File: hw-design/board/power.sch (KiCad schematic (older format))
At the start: 14 parts, among them CN1 CONN_02X02, CN2 CONN_02X02, U1 AP1117E50, U2 AP1117E33

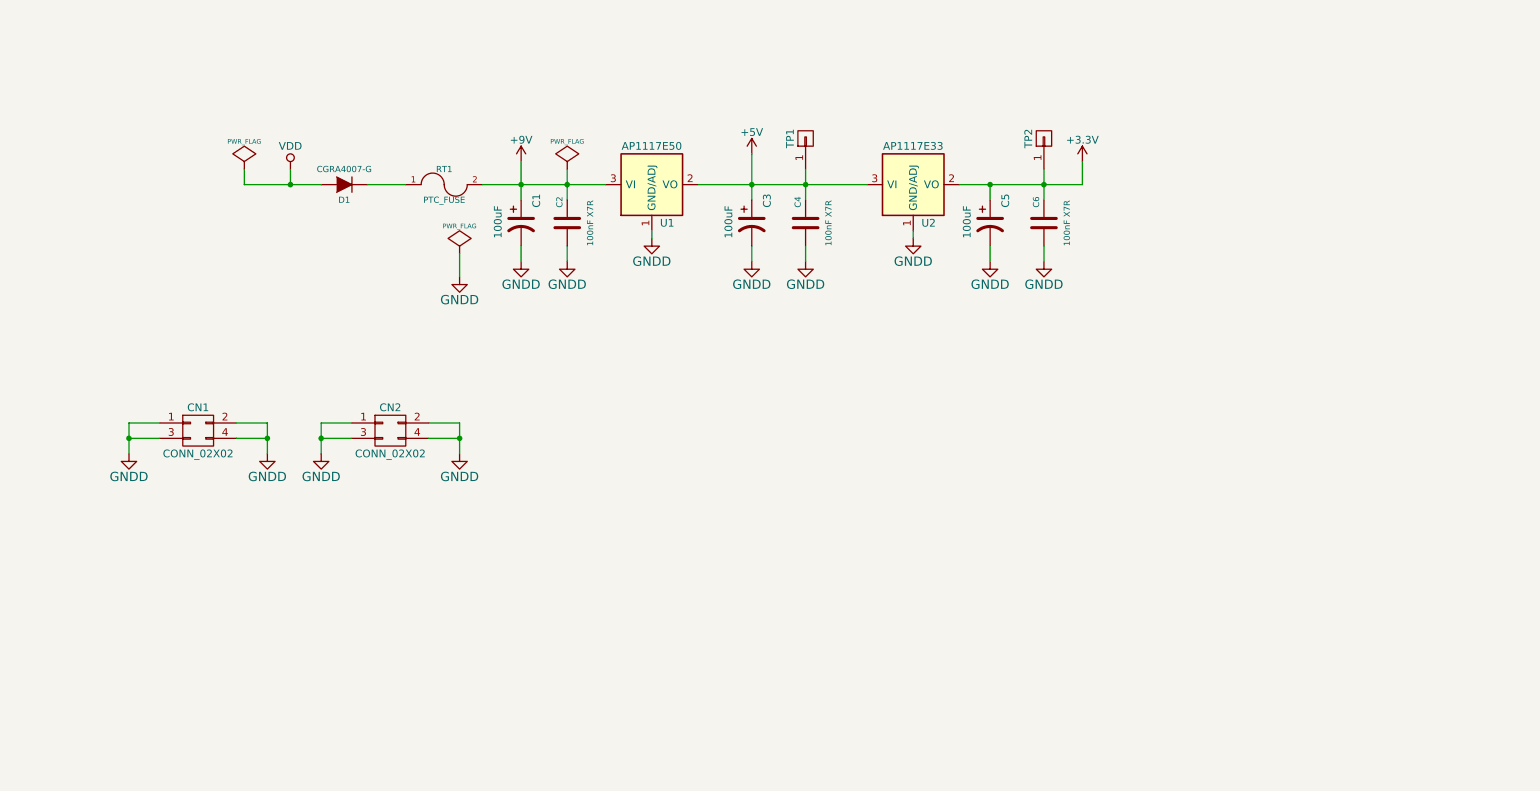
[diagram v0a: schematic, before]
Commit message: sch: load switch circuit sketch
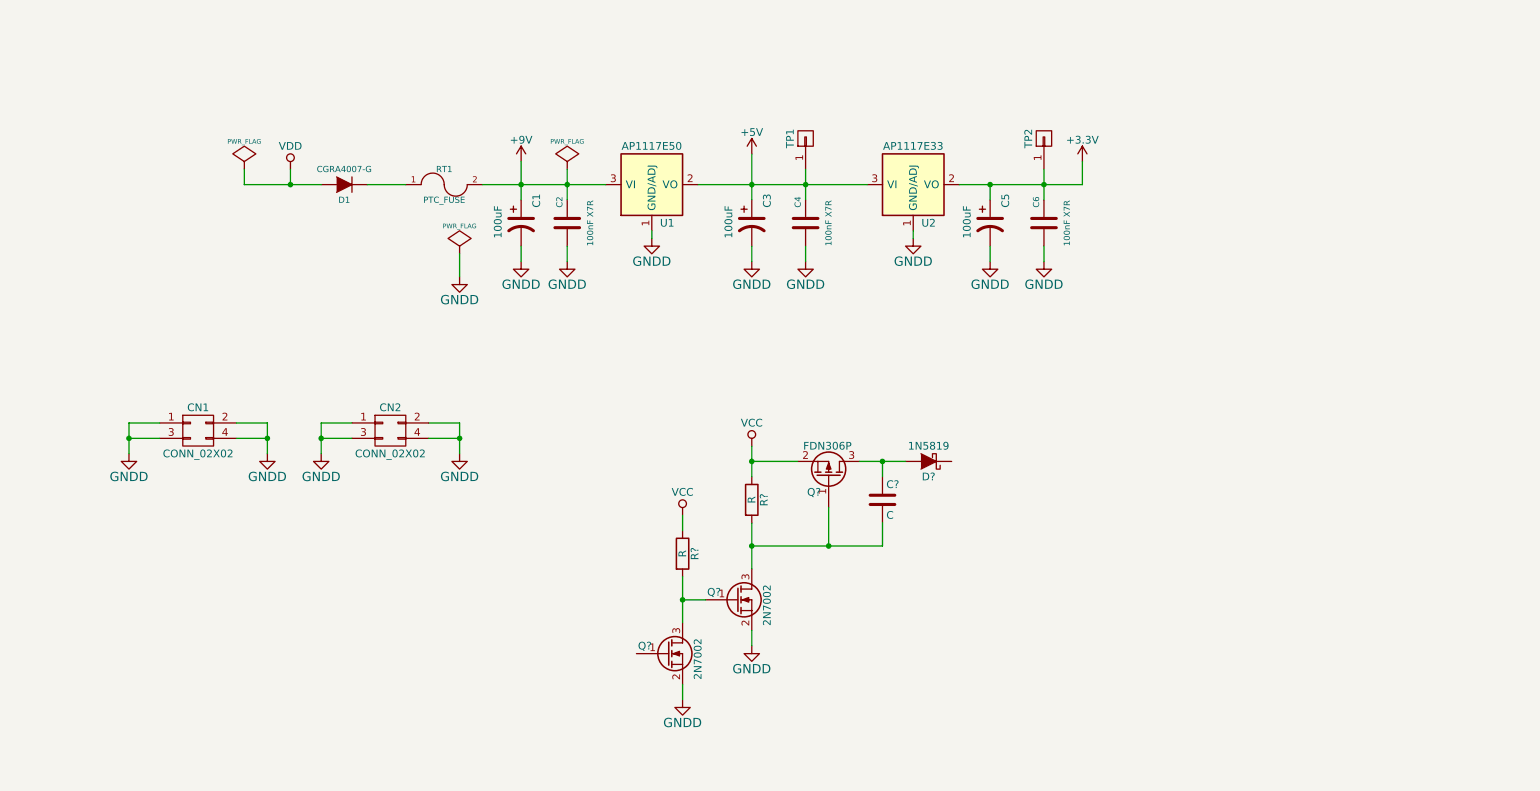
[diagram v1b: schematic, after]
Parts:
- added C?: C, symbol C
- added D?: 1N5819, symbol D_Schottky
- added Q?: FDN306P, symbol Q_PMOS_GSD
- added Q? (x2): 2N7002, symbol Q_NMOS_GSD
- added R? (x2): R, symbol R
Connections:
- net GNDD: now also Q?.2 (S), Q?.2 (S)
- new net: C?.2, Q?.1 (G), Q?.3 (D), R?.2
- new net: C?.1, D?.2 (A), Q?.3 (D)
- new net: Q?.1 (G), Q?.3 (D), R?.2
- new net VCC: Q?.2 (S), R?.1, R?.1
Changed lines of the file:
@@
 EESchema Schematic File Version 2
+LIBS:conn
+LIBS:device
+LIBS:interface
+LIBS:power
 LIBS:regul
-LIBS:power
-LIBS:device
 LIBS:transistors
 LIBS:nxp_armmcu
-LIBS:conn
-LIBS:interface
 LIBS:expression-pedal-cache
 EELAYER 25 0
@@
 	7100 2000 7100 2100
 Wire Wire Line
-	7450 1900 7450 2100
+	7450 1900 7450 2000
+Wire Wire Line
+	7450 2000 7450 2100
 Connection ~ 7100 2000
 Connection ~ 5550 2000
@@
 	4050 2400 4050 2500
 Wire Wire Line
-	4050 1850 4050 2100
+	4050 1850 4050 2000
+Wire Wire Line
+	4050 2000 4050 2100
 Connection ~ 4050 2000
 Wire Wire Line
 	4350 2400 4350 2500
 Wire Wire Line
-	4350 1900 4350 2100
+	4350 1900 4350 2000
+Wire Wire Line
+	4350 2000 4350 2100
 Connection ~ 4350 2000
 Wire Wire Line
 	3050 2000 3300 2000
 Wire Wire Line
-	5900 1900 5900 2100
+	5900 1900 5900 2000
+Wire Wire Line
+	5900 2000 5900 2100
 Connection ~ 5900 2000
 Wire Wire Line
-	5550 1800 5550 2100
-Wire Wire Line
-	2250 2000 2750 2000
+	5550 1800 5550 2000
+Wire Wire Line
+	5550 2000 5550 2100
+Wire Wire Line
+	2250 2000 2550 2000
+Wire Wire Line
+	2550 2000 2750 2000
 Wire Wire Line
 	3650 2450 3650 2600
@@
 	1500 3650 1700 3650
 Wire Wire Line
-	1500 3550 1500 3750
+	1500 3550 1500 3650
+Wire Wire Line
+	1500 3650 1500 3750
 Wire Wire Line
 	1500 3550 1700 3550
@@
 	2200 3650 2400 3650
 Wire Wire Line
-	2400 3550 2400 3750
+	2400 3550 2400 3650
+Wire Wire Line
+	2400 3650 2400 3750
 Wire Wire Line
 	2200 3550 2400 3550
 Connection ~ 2400 3650
 Wire Wire Line
-	3650 3550 3650 3750
+	3650 3550 3650 3650
+Wire Wire Line
+	3650 3650 3650 3750
 Wire Wire Line
 	3450 3650 3650 3650
@@
 	2750 3650 2950 3650
 Wire Wire Line
-	2750 3550 2750 3750
+	2750 3550 2750 3650
+Wire Wire Line
+	2750 3650 2750 3750
 Wire Wire Line
 	2750 3550 2950 3550
@@
 $EndComp
 Wire Wire Line
-	5200 2000 6300 2000
+	5200 2000 5550 2000
+Wire Wire Line
+	5550 2000 5900 2000
+Wire Wire Line
+	5900 2000 6300 2000
 $Comp
 L GNDD #PWR019
@@
 $EndComp
 Wire Wire Line
-	3800 2000 4600 2000
-Wire Wire Line
-	6900 2000 7700 2000
+	3800 2000 4050 2000
+Wire Wire Line
+	4050 2000 4350 2000
+Wire Wire Line
+	4350 2000 4600 2000
+Wire Wire Line
+	6900 2000 7100 2000
+Wire Wire Line
+	7100 2000 7450 2000
+Wire Wire Line
+	7450 2000 7700 2000
 $Comp
 L +3.3V #PWR?
@@
 	1    0    0    -1
 $EndComp
+$Comp
+L Q_PMOS_GSD Q?
+U 1 1 5576EC7B
+P 6050 3900
+F 0 "Q?" V 5950 3850 50  0000 R CNN
+F 1 "FDN306P" V 6250 4050 50  0000 R CNN
+F 2 "" H 6250 4000 29  0000 C CNN
+F 3 "" H 6050 3900 60  0000 C CNN
+	1    6050 3900
+	0    1    -1   0
+$EndComp
+$Comp
+L D_Schottky D?
+U 1 1 5576EF8F
+P 6700 3800
+F 0 "D?" H 6700 3900 50  0000 C CNN
+F 1 "1N5819" H 6700 3700 50  0000 C CNN
+F 2 "" H 6700 3800 60  0000 C CNN
+F 3 "" H 6700 3800 60  0000 C CNN
+	1    6700 3800
+	-1   0    0    1
+$EndComp
+$Comp
+L R R?
+U 1 1 5576FA4A
+P 5550 4050
+F 0 "R?" V 5630 4050 50  0000 C CNN
+F 1 "R" V 5550 4050 50  0000 C CNN
+F 2 "" V 5480 4050 30  0000 C CNN
+F 3 "" H 5550 4050 30  0000 C CNN
+	1    5550 4050
+	1    0    0    -1
+$EndComp
+$Comp
+L VCC #PWR?
+U 1 1 55770535
+P 5550 3700
+F 0 "#PWR?" H 5550 3550 50  0001 C CNN
+F 1 "VCC" H 5550 3850 50  0000 C CNN
+F 2 "" H 5550 3700 60  0000 C CNN
+F 3 "" H 5550 3700 60  0000 C CNN
+	1    5550 3700
+	1    0    0    -1
+$EndComp
+Wire Wire Line
+	5550 3700 5550 3800
+Wire Wire Line
+	5550 3800 5550 3900
+Wire Wire Line
+	5850 3800 5550 3800
+Connection ~ 5550 3800
+Wire Wire Line
+	6250 3800 6400 3800
+Wire Wire Line
+	6400 3800 6550 3800
+$Comp
+L Q_NMOS_GSD Q?
+U 1 1 55771A8F
+P 5450 4700
+F 0 "Q?" H 5350 4750 50  0000 R CNN
+F 1 "2N7002" V 5650 4800 50  0000 R CNN
+F 2 "" H 5650 4800 29  0000 C CNN
+F 3 "" H 5450 4700 60  0000 C CNN
+	1    5450 4700
+	1    0    0    -1
+$EndComp
+$Comp
+L Q_NMOS_GSD Q?
+U 1 1 55771C8E
+P 5000 5050
+F 0 "Q?" H 4900 5100 50  0000 R CNN
+F 1 "2N7002" V 5200 5150 50  0000 R CNN
+F 2 "" H 5200 5150 29  0000 C CNN
+F 3 "" H 5000 5050 60  0000 C CNN
+	1    5000 5050
+	1    0    0    -1
+$EndComp
+$Comp
+L GNDD #PWR?
+U 1 1 557724D6
+P 5100 5350
+F 0 "#PWR?" H 5100 5100 60  0001 C CNN
+F 1 "GNDD" H 5100 5200 60  0000 C CNN
+F 2 "" H 5100 5350 60  0000 C CNN
+F 3 "" H 5100 5350 60  0000 C CNN
+	1    5100 5350
+	1    0    0    -1
+$EndComp
+Wire Wire Line
+	5100 5350 5100 5250
+Wire Wire Line
+	5100 4550 5100 4700
+Wire Wire Line
+	5100 4700 5100 4850
+Wire Wire Line
+	5100 4700 5250 4700
+$Comp
+L GNDD #PWR?
+U 1 1 55772F70
+P 5550 5000
+F 0 "#PWR?" H 5550 4750 60  0001 C CNN
+F 1 "GNDD" H 5550 4850 60  0000 C CNN
+F 2 "" H 5550 5000 60  0000 C CNN
+F 3 "" H 5550 5000 60  0000 C CNN
+	1    5550 5000
+	1    0    0    -1
+$EndComp
+Wire Wire Line
+	5550 5000 5550 4900
+$Comp
+L R R?
+U 1 1 55773BAE
+P 5100 4400
+F 0 "R?" V 5180 4400 50  0000 C CNN
+F 1 "R" V 5100 4400 50  0000 C CNN
+F 2 "" V 5030 4400 30  0000 C CNN
+F 3 "" H 5100 4400 30  0000 C CNN
+	1    5100 4400
+	1    0    0    -1
+$EndComp
+Connection ~ 5100 4700
+Wire Wire Line
+	5550 4200 5550 4350
+Wire Wire Line
+	5550 4350 5550 4500
+Wire Wire Line
+	5550 4350 6050 4350
+Wire Wire Line
+	6050 4350 6400 4350
+Wire Wire Line
+	6050 4350 6050 4100
+Connection ~ 5550 4350
+$Comp
+L VCC #PWR?
+U 1 1 55774D84
+P 5100 4150
+F 0 "#PWR?" H 5100 4000 50  0001 C CNN
+F 1 "VCC" H 5100 4300 50  0000 C CNN
+F 2 "" H 5100 4150 60  0000 C CNN
+F 3 "" H 5100 4150 60  0000 C CNN
+	1    5100 4150
+	1    0    0    -1
+$EndComp
+$Comp
+L C C?
+U 1 1 55779079
+P 6400 4050
+F 0 "C?" H 6425 4150 50  0000 L CNN
+F 1 "C" H 6425 3950 50  0000 L CNN
+F 2 "" H 6438 3900 30  0000 C CNN
+F 3 "" H 6400 4050 60  0000 C CNN
+	1    6400 4050
+	1    0    0    -1
+$EndComp
+Wire Wire Line
+	6400 3900 6400 3800
+Connection ~ 6400 3800
+Wire Wire Line
+	6400 4350 6400 4200
+Connection ~ 6050 4350
+Wire Wire Line
+	5100 4250 5100 4150
 $EndSCHEMATC

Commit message: power circuit done
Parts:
- removed CN1, CN2: CONN_02X02, MOD_Footprints:CONN_PANNEL, symbol CONN_02X02
- removed TP1, TP2: ~, Pin_Headers:Pin_Header_Straight_1x01, symbol CONN_01X01
- removed U1: AP1117E50, SMD_Packages:SOT-223, symbol AP1117E50
- removed U2: AP1117E33, SMD_Packages:SOT-223, symbol AP1117E33
- added C?: 100nF X7R, Capacitors_SMD:C_0603, symbol C
- added D?: 1N5819, symbol D_Schottky
- added R? (x2): R, symbol R
- added U?: NCP1117DT50G, symbol NCP1117ST50T3G
- added U?: NCP1117DT33G, symbol NCP1117ST33T3G
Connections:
- net +3V3: now also U?.2 (VO)
- net +5V: now also D?.1 (K), C?.1, D?.1 (K), U?.3 (VI); no longer C3.1, C4.1
- net GNDD: now also C?.2, R?.2, U?.1 (GND), U?.1 (GND)
- net at Q?.1 (G): now also R?.1, R?.2
- net +9V: no longer names the net of C1.1, C2.1, RT1.2
- net +9V: now also U?.3 (VI)
- net VDD renamed POWER_INPUT
- net POWER_INPUT: now also R?.1
- new net: C3.1, C4.1, D?.2 (A), U?.2 (VO)
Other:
- note added: "CONTROL CHAIN POWER"
- note added: "USB POWER"
- moved on the sheet: C1, C2, C3, C4, C5, C6, C?, D1, D?, Q?, R?, RT1

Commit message: sch: schematic annotation done
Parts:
- gave numbers to parts that had none: 13
- renumbered C2 to C3, C3 to C4, C4 to C5, C5 to C7, C6 to C8

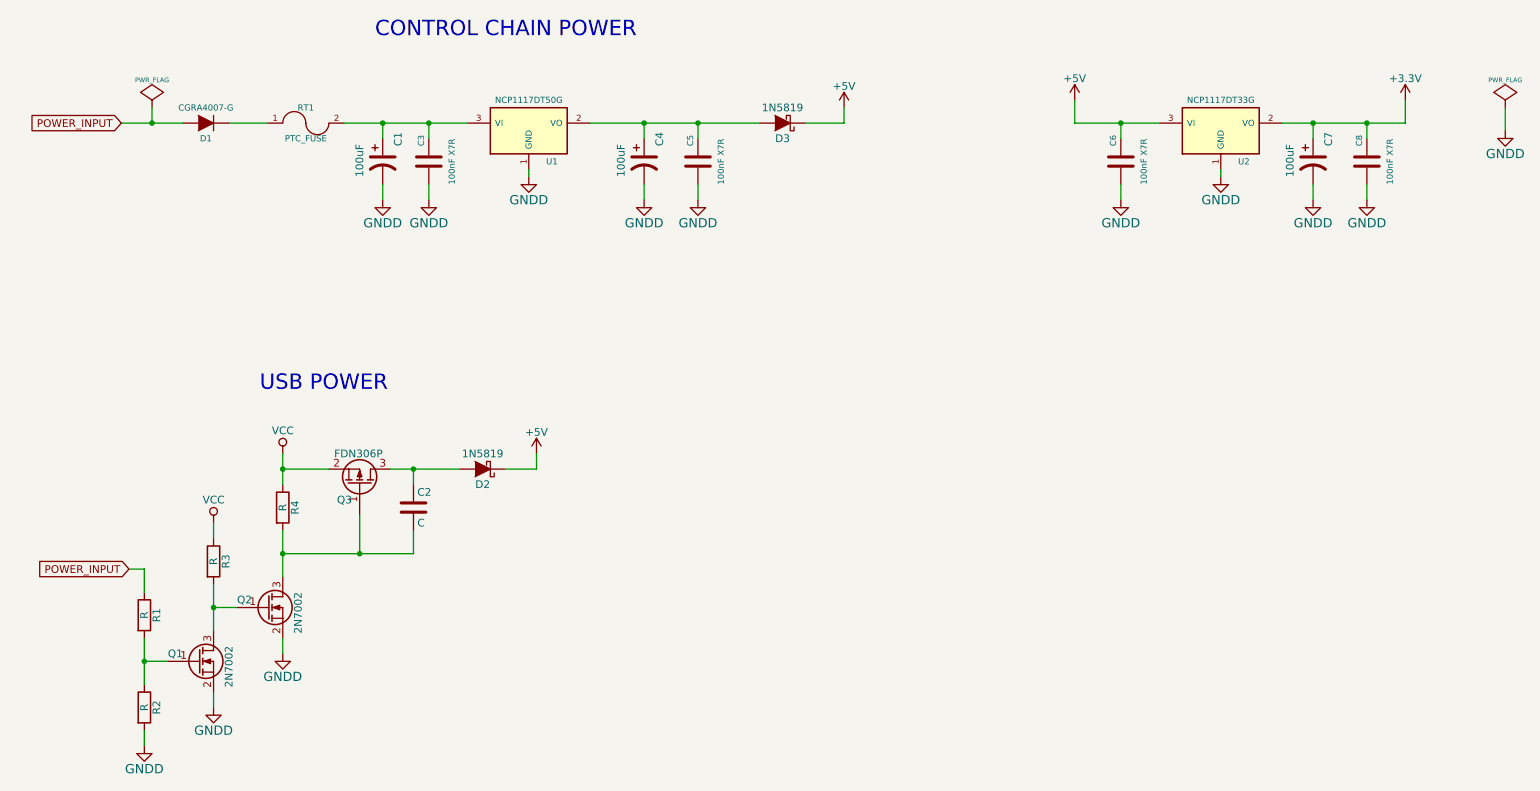
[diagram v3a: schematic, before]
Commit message: sch: errors fixed, DRC passing
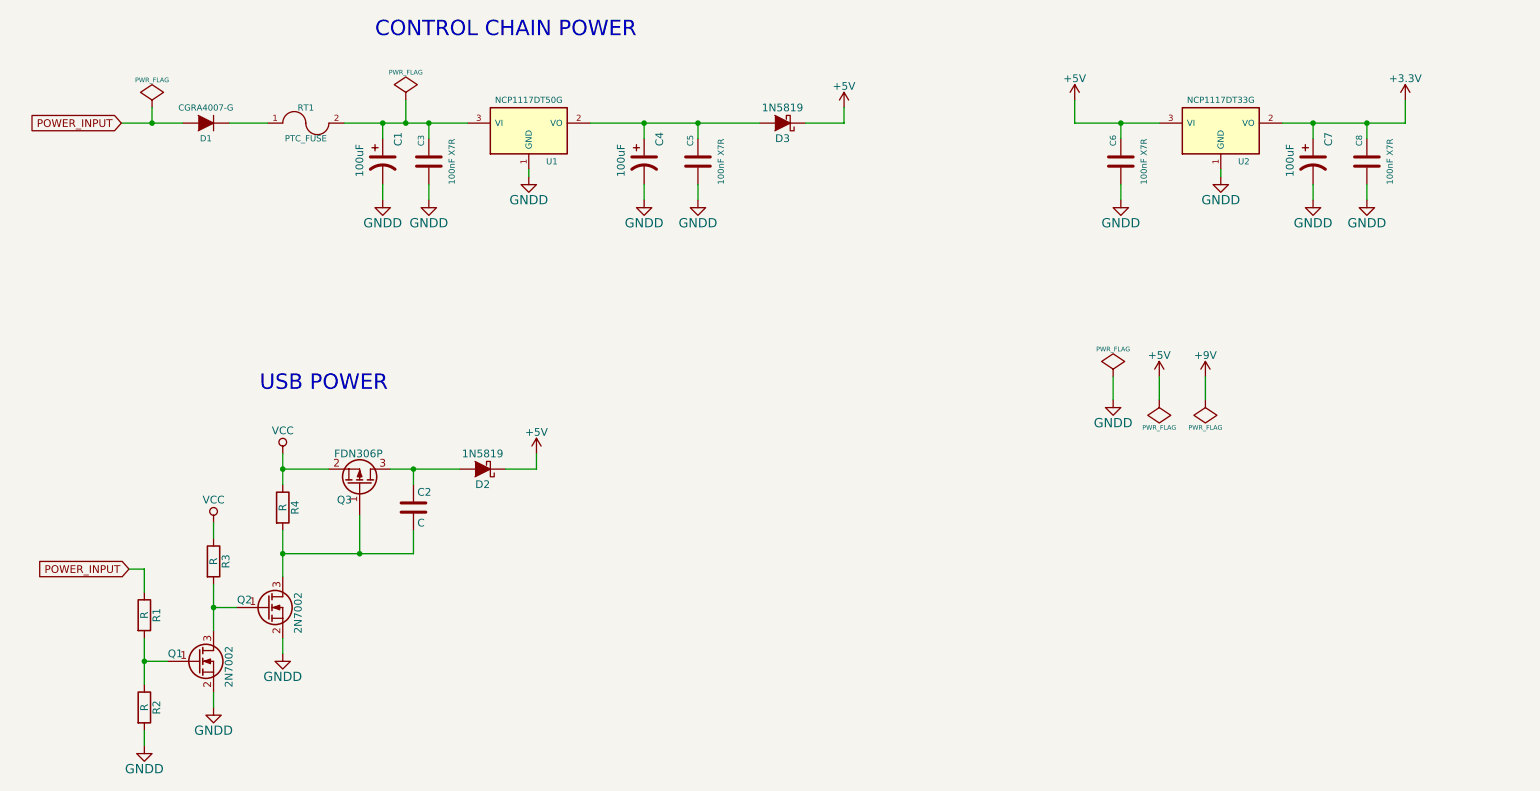
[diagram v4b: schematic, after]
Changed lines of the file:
@@
 L PWR_FLAG #FLG01
 U 1 1 54B500E8
-P 10450 1500
-F 0 "#FLG01" H 10450 1595 30  0001 C CNN
-F 1 "PWR_FLAG" H 10450 1680 30  0000 C CNN
-F 2 "" H 10450 1500 60  0000 C CNN
-F 3 "" H 10450 1500 60  0000 C CNN
-	1    10450 1500
+P 7900 3250
+F 0 "#FLG01" H 7900 3345 30  0001 C CNN
+F 1 "PWR_FLAG" H 7900 3430 30  0000 C CNN
+F 2 "" H 7900 3250 60  0000 C CNN
+F 3 "" H 7900 3250 60  0000 C CNN
+	1    7900 3250
 	1    0    0    -1
 $EndComp
@@
 L GNDD #PWR03
 U 1 1 54E7EDE1
-P 10450 1650
-F 0 "#PWR03" H 10450 1400 60  0001 C CNN
-F 1 "GNDD" H 10450 1500 60  0000 C CNN
-F 2 "" H 10450 1650 60  0000 C CNN
-F 3 "" H 10450 1650 60  0000 C CNN
-	1    10450 1650
+P 7900 3400
+F 0 "#PWR03" H 7900 3150 60  0001 C CNN
+F 1 "GNDD" H 7900 3250 60  0000 C CNN
+F 2 "" H 7900 3400 60  0000 C CNN
+F 3 "" H 7900 3400 60  0000 C CNN
+	1    7900 3400
 	1    0    0    -1
 $EndComp
@@
 	1450 1600 1850 1600
 Wire Wire Line
-	10450 1500 10450 1650
+	7900 3250 7900 3400
 Wire Wire Line
 	1650 1500 1650 1600
@@
 Wire Wire Line
 	1600 4500 1600 4650
+$Comp
+L PWR_FLAG #FLG022
+U 1 1 557B2C54
+P 3300 1450
+F 0 "#FLG022" H 3300 1545 30  0001 C CNN
+F 1 "PWR_FLAG" H 3300 1630 30  0000 C CNN
+F 2 "" H 3300 1450 60  0000 C CNN
+F 3 "" H 3300 1450 60  0000 C CNN
+	1    3300 1450
+	1    0    0    -1
+$EndComp
+Wire Wire Line
+	3300 1450 3300 1600
+Connection ~ 3300 1600
+$Comp
+L PWR_FLAG #FLG023
+U 1 1 557B3123
+P 8200 3400
+F 0 "#FLG023" H 8200 3495 30  0001 C CNN
+F 1 "PWR_FLAG" H 8200 3580 30  0000 C CNN
+F 2 "" H 8200 3400 60  0000 C CNN
+F 3 "" H 8200 3400 60  0000 C CNN
+	1    8200 3400
+	-1   0    0    1
+$EndComp
+$Comp
+L +5V #PWR024
+U 1 1 557B3200
+P 8200 3250
+F 0 "#PWR024" H 8200 3100 50  0001 C CNN
+F 1 "+5V" H 8200 3390 50  0000 C CNN
+F 2 "" H 8200 3250 60  0000 C CNN
+F 3 "" H 8200 3250 60  0000 C CNN
+	1    8200 3250
+	1    0    0    -1
+$EndComp
+Wire Wire Line
+	8200 3250 8200 3400
+$Comp
+L PWR_FLAG #FLG?
+U 1 1 557B4378
+P 8500 3400
+F 0 "#FLG?" H 8500 3495 30  0001 C CNN
+F 1 "PWR_FLAG" H 8500 3580 30  0000 C CNN
+F 2 "" H 8500 3400 60  0000 C CNN
+F 3 "" H 8500 3400 60  0000 C CNN
+	1    8500 3400
+	-1   0    0    1
+$EndComp
+Wire Wire Line
+	8500 3250 8500 3400
+$Comp
+L +9V #PWR?
+U 1 1 557B43C7
+P 8500 3250
+F 0 "#PWR?" H 8500 3100 50  0001 C CNN
+F 1 "+9V" H 8500 3390 50  0000 C CNN
+F 2 "" H 8500 3250 60  0000 C CNN
+F 3 "" H 8500 3250 60  0000 C CNN
+	1    8500 3250
+	1    0    0    -1
+$EndComp
 $EndSCHEMATC
